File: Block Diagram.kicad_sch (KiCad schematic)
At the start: 0 parts

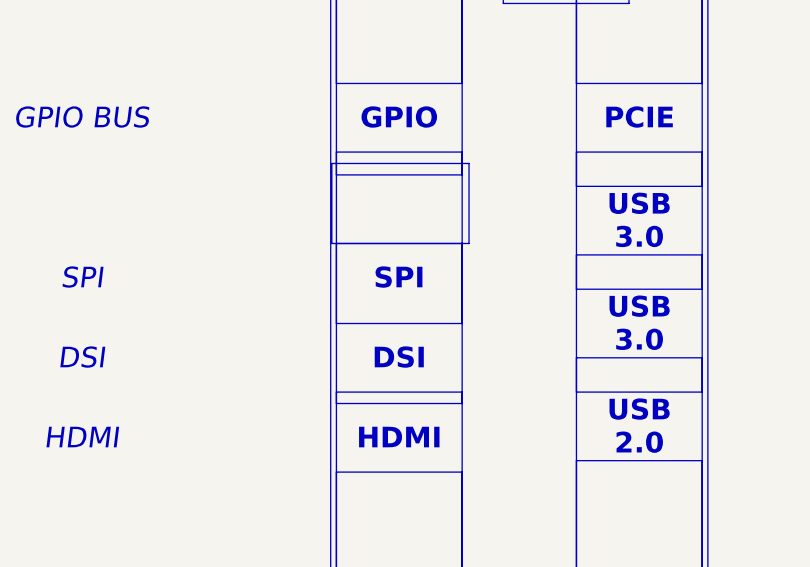
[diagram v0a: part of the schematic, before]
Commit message: Drives moved
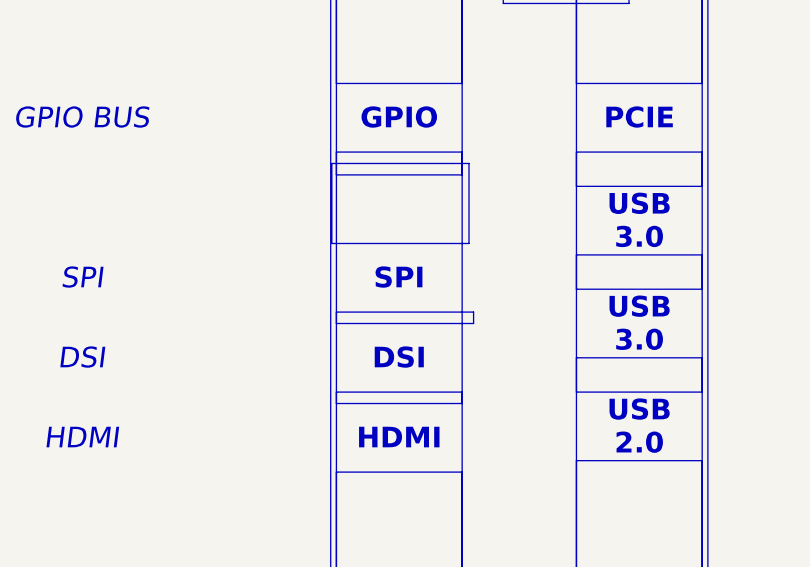
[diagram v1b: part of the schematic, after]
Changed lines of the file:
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@@
-	)
-	(rectangle
-		(start 241.3 130.81)
-		(end 255.27 139.7)
-		(stroke
-			(width 0)
-			(type default)
-			(color 26 179 18 1)
-		)
-		(fill
-			(type color)
-			(color 26 179 18 1)
-		)
 	)
 	(rectangle
@@
 		)
 	)
+	(rectangle
+		(start 241.3 138.43)
+		(end 256.54 139.7)
+		(stroke
+			(width 0)
+			(type solid)
+			(color 26 179 18 1)
+		)
+		(fill
+			(type color)
+			(color 26 179 18 1)
+		)
+	)

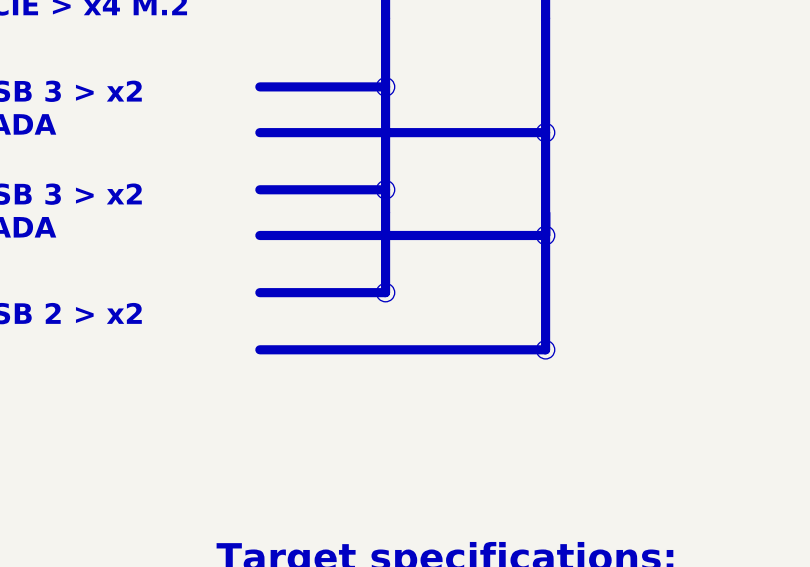
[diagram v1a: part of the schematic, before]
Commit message: Sheet name edit and changed to net labels
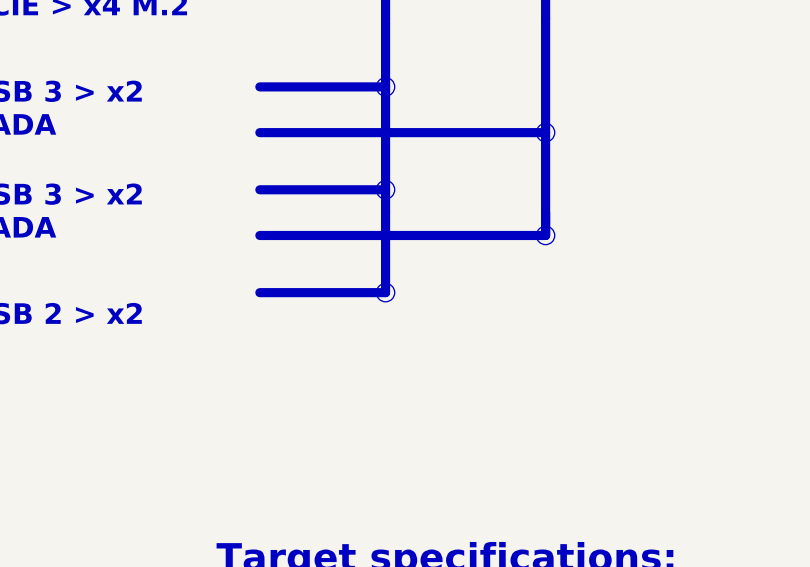
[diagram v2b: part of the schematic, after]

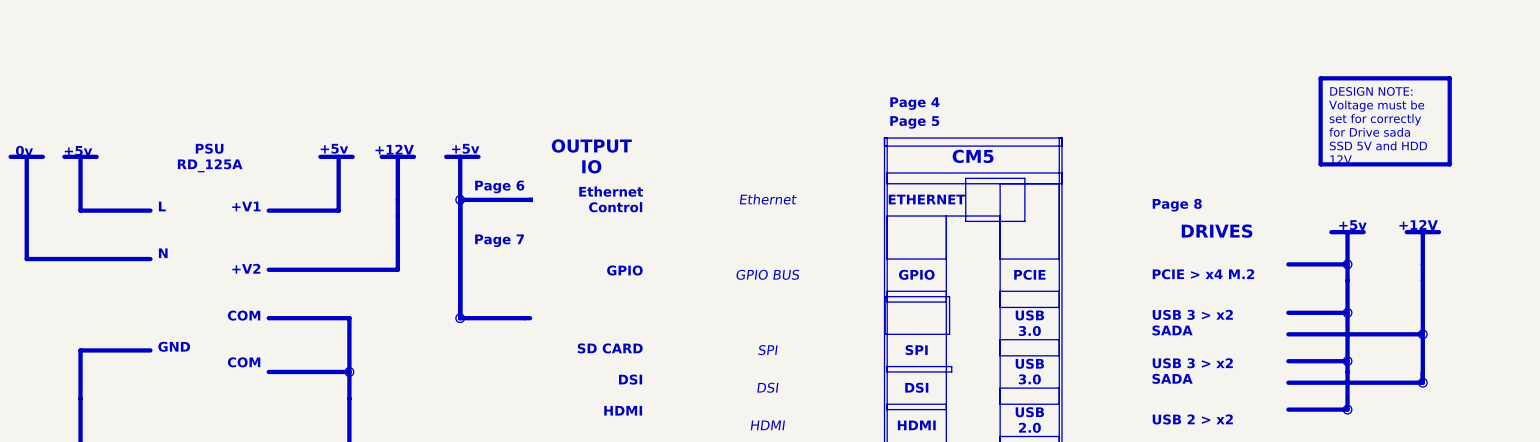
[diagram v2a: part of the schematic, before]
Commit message: Swiitched to JSM561
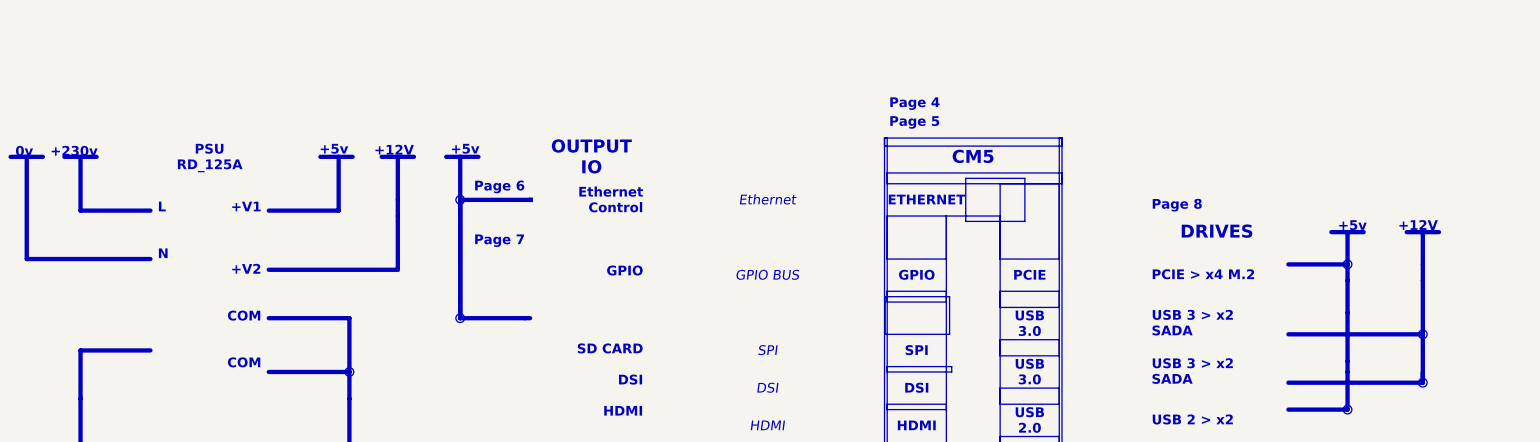
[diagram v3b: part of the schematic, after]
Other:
- note added: "+230v"
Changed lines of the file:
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@@
-		)
-	)
-	(circle
-		(center 350.012 125.73)
-		(radius 1.016)
-		(stroke
-			(width 0)
-			(type default)
-			(color 198 71 194 1)
-		)
-		(fill
-			(type color)
-			(color 198 71 194 1)
 		)
 	)
@@
 		)
 	)
-	(circle
-		(center 350.012 137.16)
-		(radius 1.016)
-		(stroke
-			(width 0)
-			(type default)
-			(color 198 71 194 1)
-		)
-		(fill
-			(type color)
-			(color 198 71 194 1)
-		)
-	)
 	(rectangle
 		(start 281.94 84.455)
@@
 		)
 	)
-	(text "+5v"
-		(exclude_from_sim no)
-		(at 53.594 89.154 0)
+	(text "+230v"
+		(exclude_from_sim no)
+		(at 54.864 89.154 0)
 		(effects
 			(font
@@
 		)
 	)
-	(text_box "\nL\n\n\nN\n\n\n\n\n\nGND"
+	(text_box "\nL\n\n\nN\n\n\n\n\n\n"
 		(exclude_from_sim no)
 		(at 67.31 93.98 0)
@@
 		)
 	)
-	(text_box "DESIGN NOTE:\nVoltage must be set for correctly for Drive sada SSD 5V and HDD 12V"
-		(exclude_from_sim no)
-		(at 343.662 70.358 0)
-		(size 30.48 20.32)
-		(margins 2 2 2 2)
-		(stroke
-			(width 1)
-			(type solid)
-			(color 255 0 0 1)
-		)
-		(fill
-			(type none)
-		)
-		(effects
-			(font
-				(face "Arial")
-				(size 2 2)
-				(color 255 0 0 1)
-			)
-			(justify left top)
-		)
-	)
 	(text_box "PSU RD_125A"
 		(exclude_from_sim no)
@@
 	(polyline
 		(pts
-			(xy 336.042 125.73) (xy 350.012 125.73)
-		)
-		(stroke
-			(width 1.016)
-			(type solid)
-			(color 198 71 194 1)
-		)
-	)
-	(polyline
-		(pts
 			(xy 367.792 142.24) (xy 367.792 139.7)
 		)
@@
 		)
 	)
-	(polyline
-		(pts
-			(xy 336.042 137.16) (xy 350.012 137.16)
-		)
-		(stroke
-			(width 1.016)
-			(type solid)
-			(color 198 71 194 1)
-		)
-	)

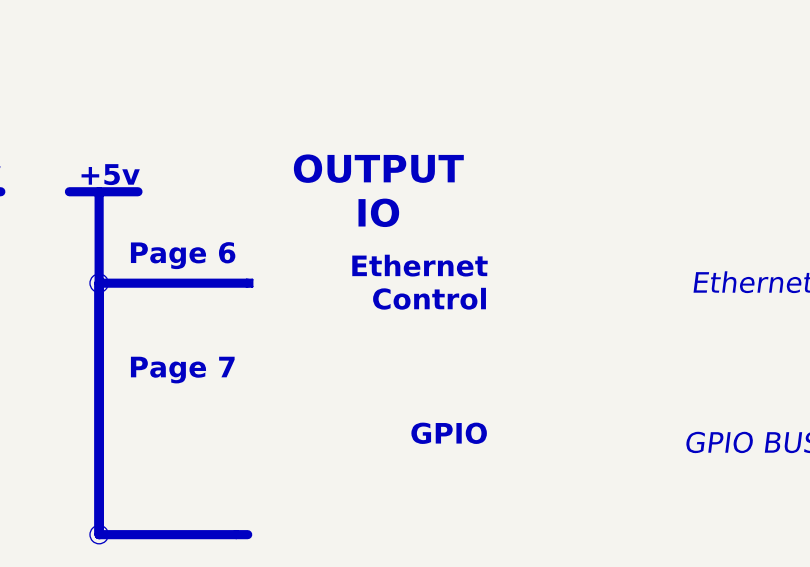
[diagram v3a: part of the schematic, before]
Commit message: Removed Ethernet
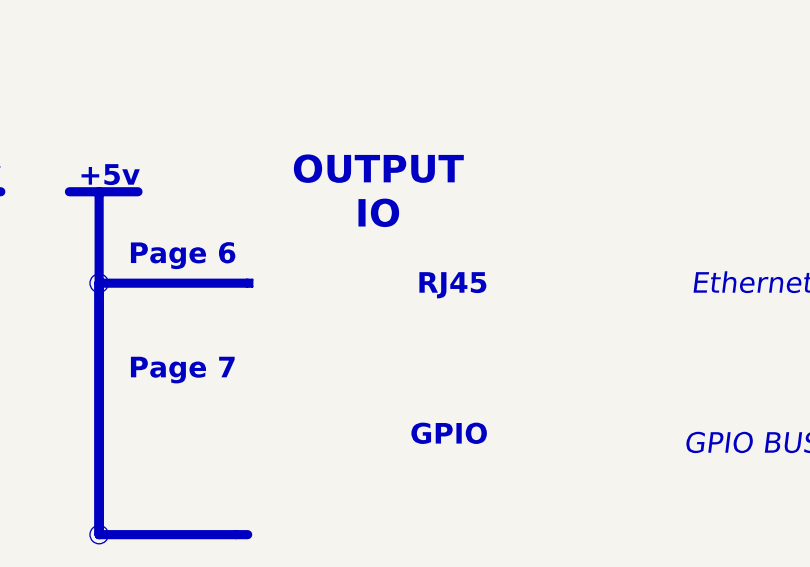
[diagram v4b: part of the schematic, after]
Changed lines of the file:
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@@
 		)
 	)
-	(text_box "Ethernet Control"
+	(text_box "RJ45\n"
 		(exclude_from_sim no)
 		(at 157.48 93.98 0)
